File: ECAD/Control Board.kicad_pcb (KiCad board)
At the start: 2 copper layers, 184.2 x 57.8 mm, 60 parts, among them J3 Thermocouple, J4 SD_Card, J5 PWR/Heat, J7 UPDI, Q1 IPD50N06S4L08, SW1 Reflow, SW2 Stop, SW3 Set temp mode, U1 ATtiny1614-SS, U2 TPS7B8833QKVURQ1, U3 AD8497, U4 HT16K33

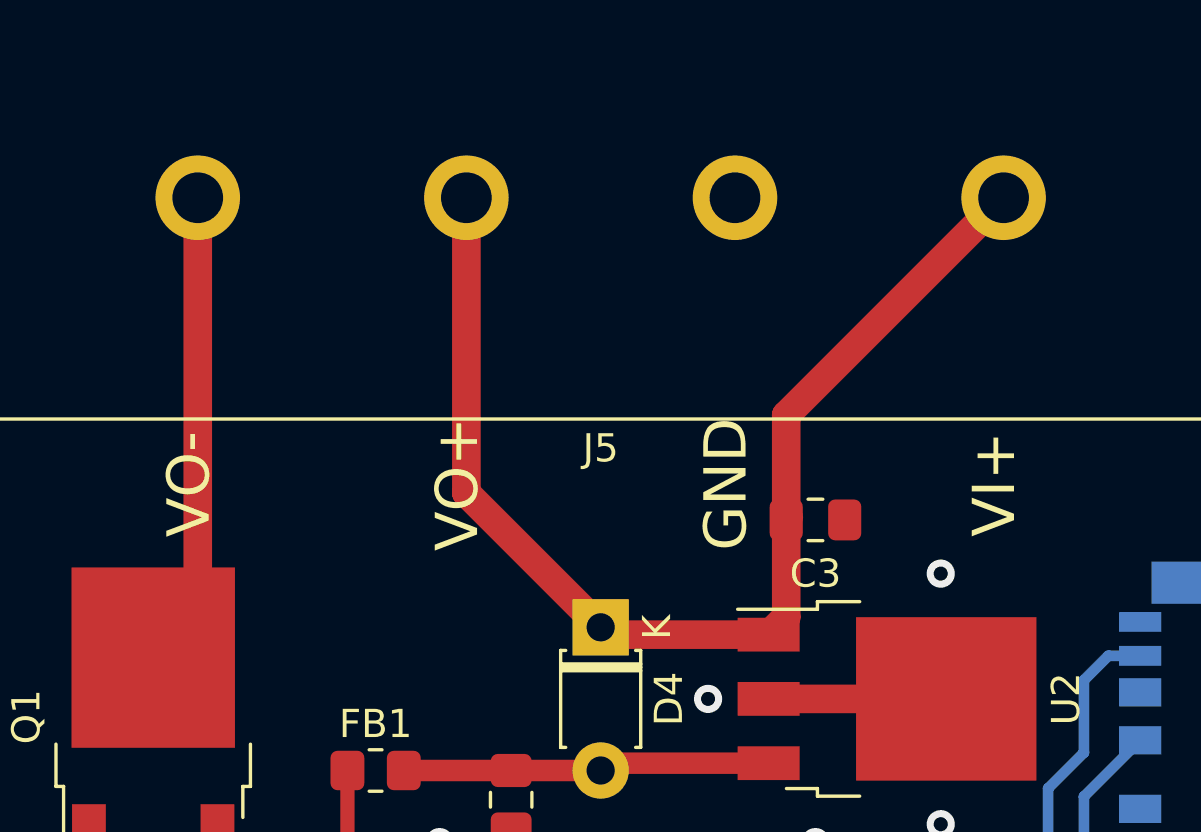
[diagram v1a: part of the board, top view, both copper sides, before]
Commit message: High voltage modifications
Widened high voltage tracks and replaced schottky diode with higher back voltage diode.
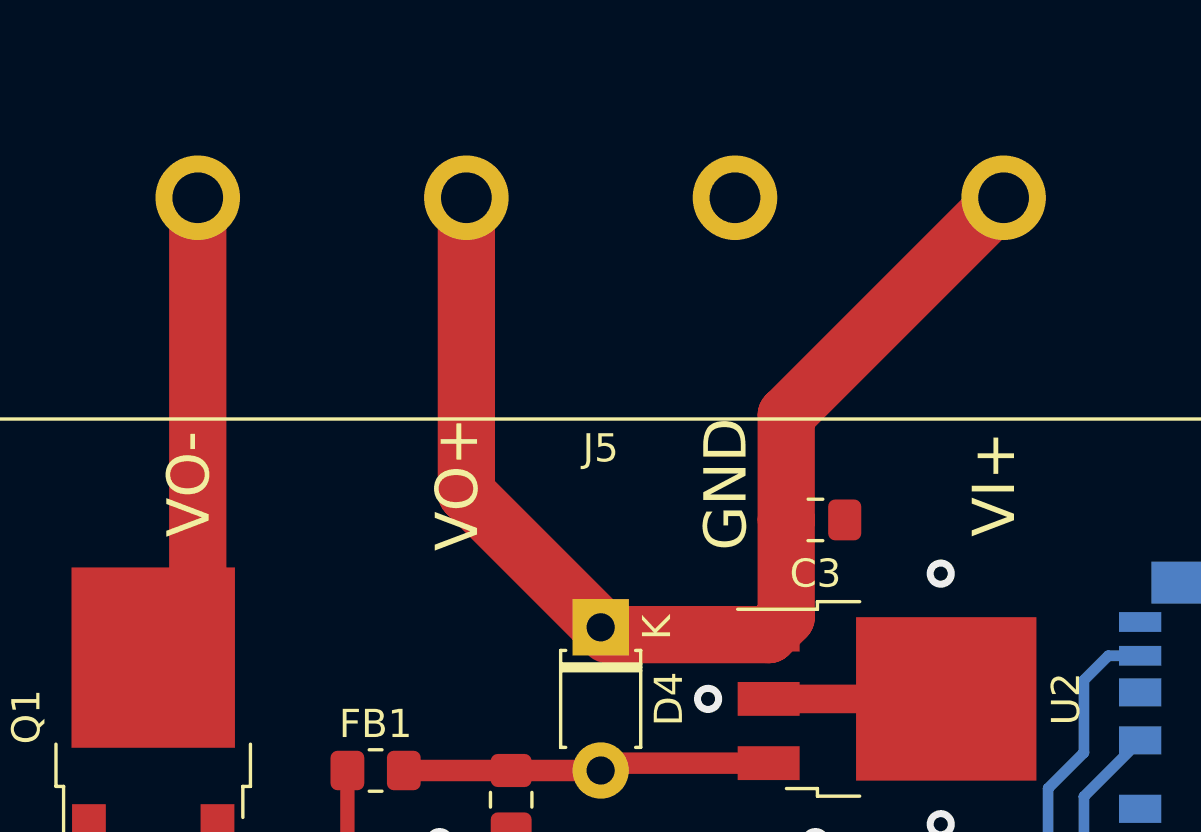
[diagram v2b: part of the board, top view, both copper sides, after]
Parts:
- D4: value 1N5818 -> 1N5711
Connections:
- DS1 pad 3: (no net) -> Net-(DS1-Pad3)
- DS2 pad 3: (no net) -> Net-(DS2-Pad3)
- DS3 pad 3: (no net) -> Net-(DS3-Pad3)
- J4 pad 11: (no net) -> /WRPrt
- J4 pad 8: (no net) -> Net-(J4-Pad8)
- J4 pad 9: (no net) -> Net-(J4-Pad9)
- U1 pad 6: (no net) -> Net-(U1-Pad6)
- U3 pad 4: (no net) -> Net-(U3-Pad4)
- U4 pad 10: (no net) -> Net-(U4-Pad10)
- U4 pad 11: (no net) -> Net-(U4-Pad11)
- U4 pad 8: (no net) -> Net-(U4-Pad8)
- U4 pad 9: (no net) -> Net-(U4-Pad9)

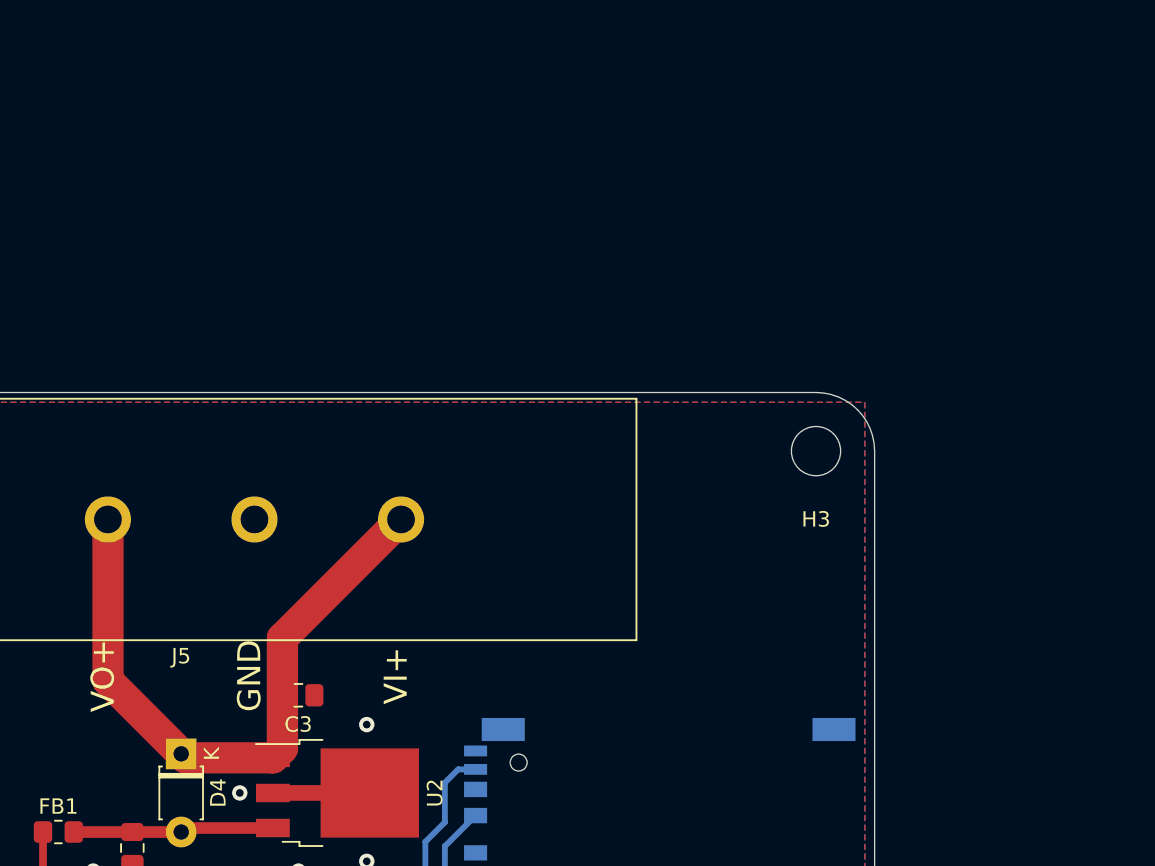
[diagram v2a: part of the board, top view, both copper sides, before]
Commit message: Added footprints to board
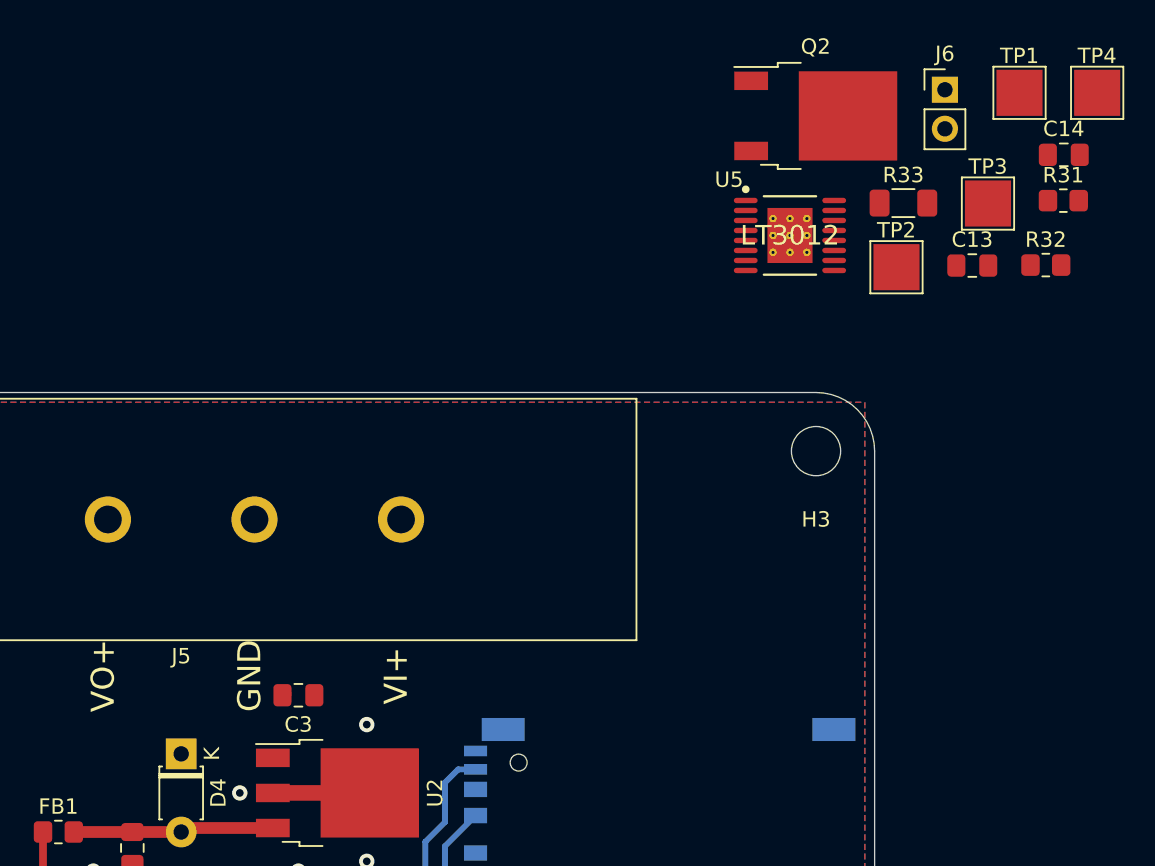
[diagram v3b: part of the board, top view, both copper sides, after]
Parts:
- added C13: 1uF, Capacitor_SMD:C_0805_2012Metric_Pad1.18x1.45mm_HandSolder, F.Cu at (240.0, 37.5)
- added C14: 4.7uF, Capacitor_SMD:C_0805_2012Metric_Pad1.18x1.45mm_HandSolder, F.Cu at (246.0, 30.3)
- added J6: FAN, Connector_PinHeader_2.54mm:PinHeader_1x02_P2.54mm_Vertical, F.Cu at (238.2, 26.0)
- added Q2: IPD50N06S4L08, Package_TO_SOT_SMD:TO-252-2, F.Cu at (229.8, 27.7)
- added R31: 1.74M, Resistor_SMD:R_0805_2012Metric_Pad1.20x1.40mm_HandSolder, F.Cu at (245.9, 33.2)
- added R32: 200K, Resistor_SMD:R_0805_2012Metric_Pad1.20x1.40mm_HandSolder, F.Cu at (244.8, 37.4)
- added R33: 100R, Resistor_SMD:R_1206_3216Metric_Pad1.30x1.75mm_HandSolder, F.Cu at (235.6, 33.4)
- added TP1: VIN, TestPoint:TestPoint_Pad_3.0x3.0mm, F.Cu at (243.1, 26.2)
- added TP2: 12V, TestPoint:TestPoint_Pad_3.0x3.0mm, F.Cu at (235.1, 37.6)
- added TP3: 3.3V, TestPoint:TestPoint_Pad_3.0x3.0mm, F.Cu at (241.1, 33.4)
- added TP4: GND, TestPoint:TestPoint_Pad_3.0x3.0mm, F.Cu at (248.2, 26.2)
- added U5: LT3012, PCB Heater:Linear_Technology-LT3012EFETRPBF-Level_B, F.Cu at (228.2, 35.5)
- C3: value 1uF -> 10uF
- U2: value TPS7B8833QKVURQ1 -> LD1086DT33
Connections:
- C3 pad 1: VCC -> +12V
- D4 pad 1: VCC -> +12V
- U1 pad 6: Net-(U1-Pad6) -> /FanPWM
- U2 pad 1: VCC -> +12V
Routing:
- net VCC: track 42.4 -> 0.00 mm

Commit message: Re-arrange components
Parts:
- TP1, TP2, TP3, TP4: footprint TestPoint:TestPoint_Pad_3.0x3.0mm -> TestPoint:TestPoint_Pad_2.0x2.0mm
- moved J6 196.1 mm to (52.1, 87.6)
- moved R33 185.5 mm to (54.4, 73.2)
- moved Q2 179.6 mm to (57.8, 79.4)
- moved TP2 33.5 mm to (258.6, 13.7)
- moved TP3 23.2 mm to (258.6, 18.3)
- moved TP1 23.1 mm to (258.6, 9.14)
- moved C13 20.1 mm to (220.0, 38.1), turned to 270 degrees
- moved R31 12.5 mm to (234.7, 38.6), turned to 270 degrees
- moved R32 12.2 mm to (234.7, 44.2), turned to 270 degrees
- moved TP4 11.0 mm to (258.6, 22.9)
- moved C14 8.89 mm to (245.4, 39.1), turned to 270 degrees
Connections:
- DS1 pad 3: Net-(DS1-Pad3) -> (no net)
- DS2 pad 3: Net-(DS2-Pad3) -> (no net)
- DS3 pad 3: Net-(DS3-Pad3) -> (no net)
- J4 pad 11: /WRPrt -> (no net)
- J4 pad 8: Net-(J4-Pad8) -> (no net)
- J4 pad 9: Net-(J4-Pad9) -> (no net)
- J5 pad 1: /H- -> GND
- J5 pad 2: VCC -> /H-
- J5 pad 3: GND -> VCC
- U3 pad 4: Net-(U3-Pad4) -> (no net)
- U4 pad 10: Net-(U4-Pad10) -> (no net)
- U4 pad 11: Net-(U4-Pad11) -> (no net)
- U4 pad 8: Net-(U4-Pad8) -> (no net)
- U4 pad 9: Net-(U4-Pad9) -> (no net)
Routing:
- net /H-: track 17.0 -> 0.00 mm
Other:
- board text added: "PCB Heater Control Board Rev 0.3"
- board text removed: "PCB Heater Control Board Rev 0.2"

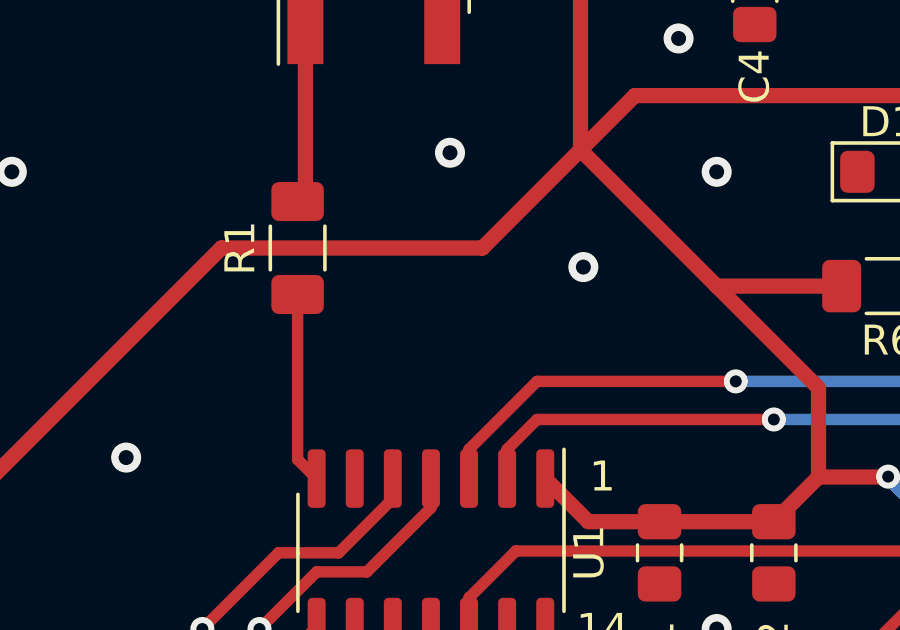
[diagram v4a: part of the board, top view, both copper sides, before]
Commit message: Added pulldown to mosfet gate
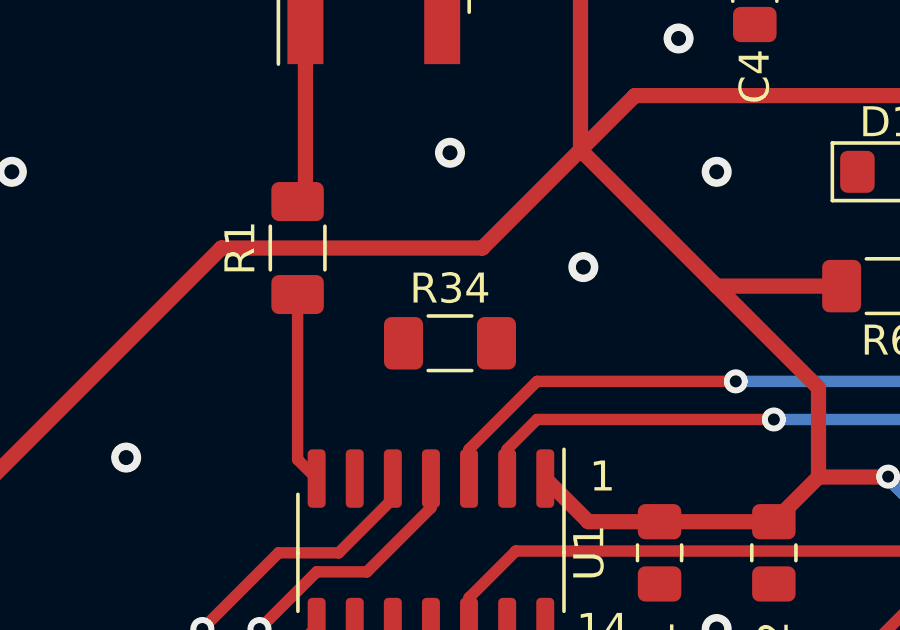
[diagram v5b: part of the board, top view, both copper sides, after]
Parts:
- added R34: 10K, Resistor_SMD:R_1206_3216Metric_Pad1.30x1.75mm_HandSolder, F.Cu at (175.3, 87.0)

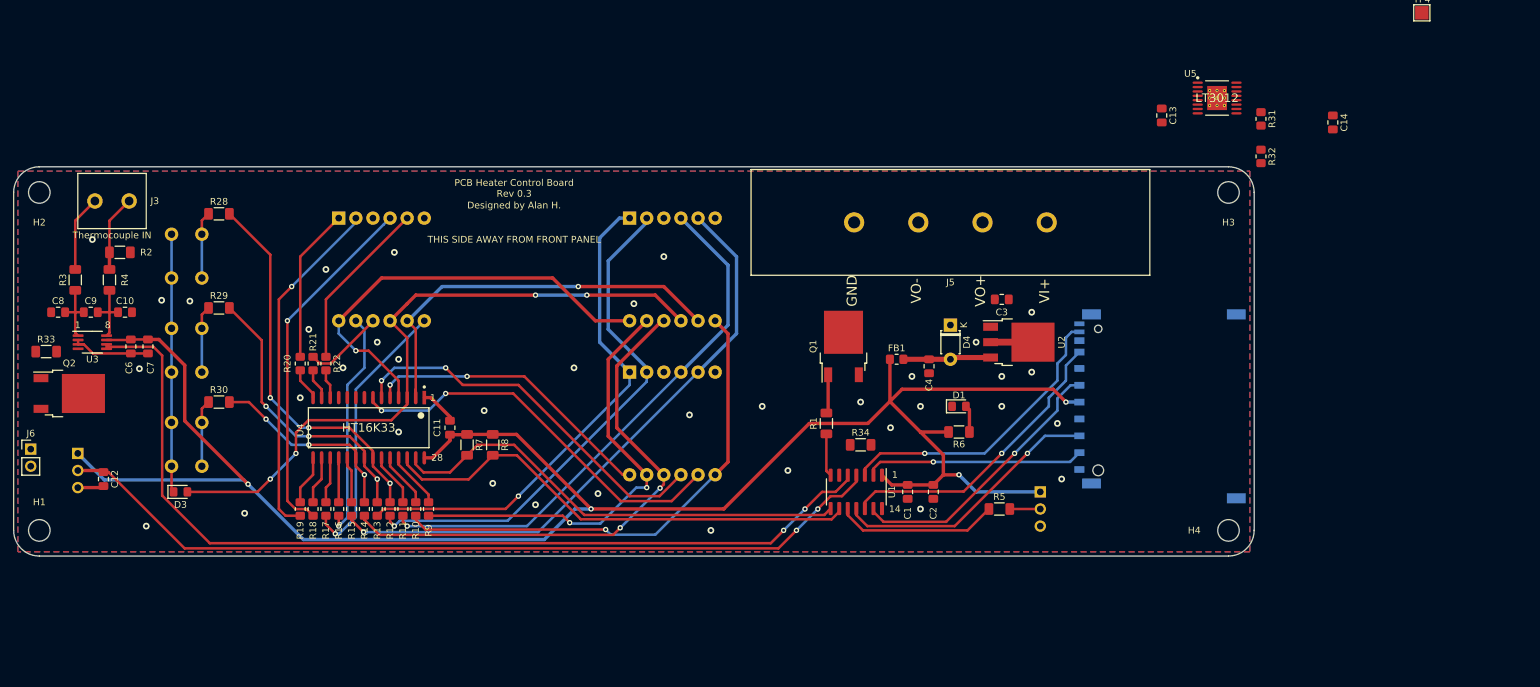
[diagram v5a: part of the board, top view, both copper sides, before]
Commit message: Replaced primary LDO with LM317
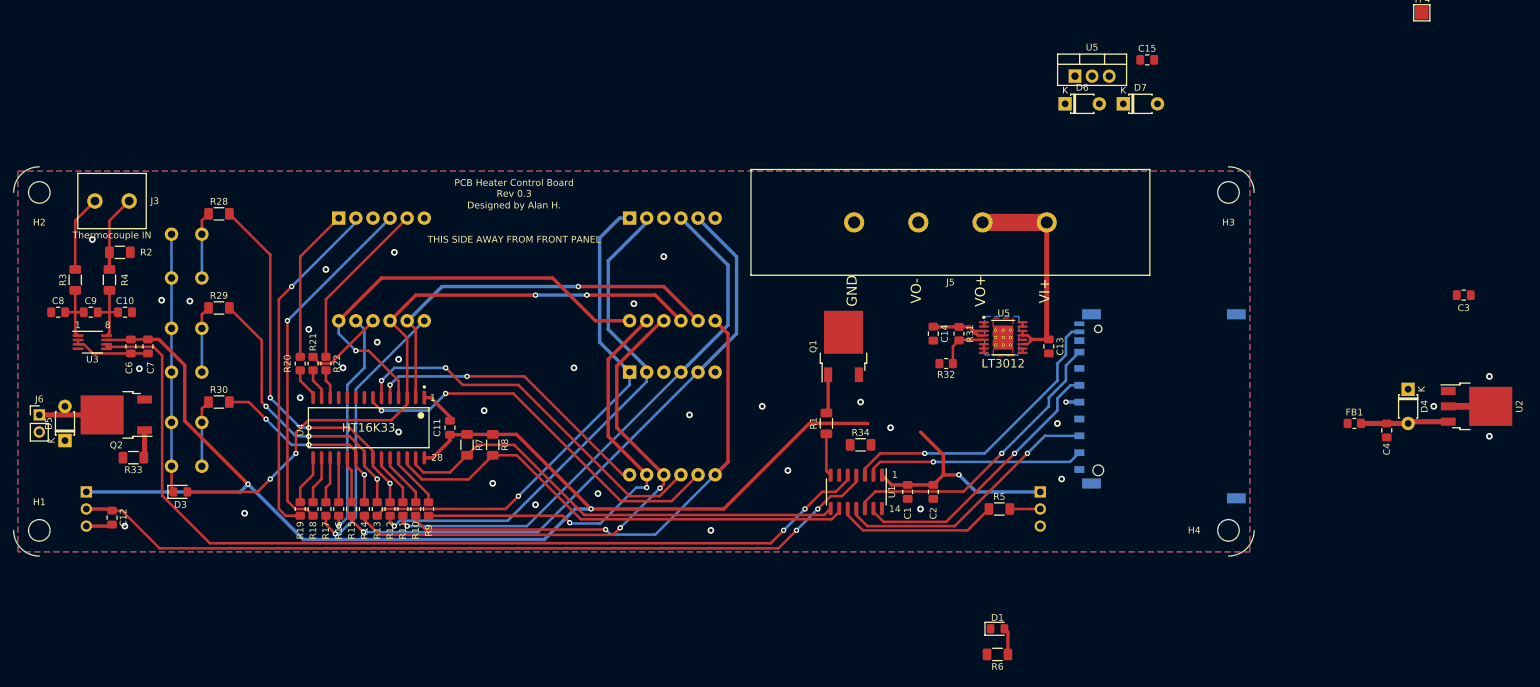
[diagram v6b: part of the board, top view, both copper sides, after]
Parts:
- removed the U5 at (228.2, 35.5)
- added C15: 10uF, Capacitor_SMD:C_0805_2012Metric_Pad1.18x1.45mm_HandSolder, F.Cu at (217.8, 29.8)
- added D5: 1N4001, Diode_THT:D_T-1_P5.08mm_Horizontal, F.Cu at (57.1, 86.4)
- added D6: 1N4002, Diode_THT:D_T-1_P5.08mm_Horizontal, F.Cu at (205.6, 36.4)
- added D7: 1N4001, Diode_THT:D_T-1_P5.08mm_Horizontal, F.Cu at (214.3, 36.4)
- added U5: LM317, Package_TO_SOT_THT:TO-220-3_Vertical, F.Cu at (207.1, 32.3)
- added U5: LT3012, PCB Heater:Linear_Technology-LT3012EFETRPBF-Level_B, F.Cu at (196.4, 71.1)
- C13: value 1uF -> 0.1uF
- R31: value 1.74M -> 240R
- R32: value 200K -> 2.1K
- moved C4 68.6 mm to (253.4, 84.9)
- moved D4 68.6 mm to (256.5, 78.7)
- moved U2 68.6 mm to (266.7, 81.3)
- moved FB1 68.6 mm to (248.6, 83.8)
- moved C3 68.6 mm to (264.8, 64.8)
- moved C14 67.1 mm to (186.1, 70.5)
- moved R32 55.9 mm to (188.0, 74.9), turned to 180 degrees
- moved R31 55.0 mm to (189.9, 70.5)
- moved C13 38.2 mm to (203.2, 72.4)
- moved D1 33.5 mm to (195.6, 114.3)
- moved R6 33.5 mm to (195.6, 118.1)
- moved R33 20.4 mm to (67.3, 88.9), turned to 180 degrees
- moved Q2 7.67 mm to (64.8, 82.5), turned to 180 degrees
- moved C12 5.85 mm to (64.1, 97.8)
- moved RV1 5.85 mm to (60.3, 94.0)
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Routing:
- net +3V3: track 280.4 -> 228.5 mm
- net VCC: track 0.00 -> 33.5 mm
- net +12V: track 0.50 -> 10.9 mm
- net Net-(D5-Pad2): track 0.00 -> 9.33 mm
- net Net-(R31-Pad2): track 0.00 -> 7.54 mm
- net Net-(Q2-Pad1): track 0.00 -> 4.12 mm
- net /TempCtrl: track 125.4 -> 121.8 mm
- net GND: track 27.4 -> 30.6 mm, vias 35 -> 31

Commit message: Associate footprints and update board
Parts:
- removed D7: 1N4001, Diode_THT:D_T-1_P5.08mm_Horizontal
- removed the U5 at (207.1, 32.3)
- removed the U5 at (196.4, 71.1)
- added L1: 470uH, Inductor_SMD:L_12x12mm_H8mm, F.Cu at (293.3, 39.5)
- added U5: LM2575HVS-ADJ, Package_TO_SOT_SMD:TO-263-5_TabPin3, F.Cu at (277.0, 38.6)
- C13: value 0.1uF -> 100uF; footprint Capacitor_SMD:C_0805_2012Metric_Pad1.18x1.45mm_HandSolder -> Capacitor_SMD:CP_Elec_10x10.5
- C14: value 4.7uF -> 470uF; footprint Capacitor_SMD:C_0805_2012Metric_Pad1.18x1.45mm_HandSolder -> Capacitor_SMD:CP_Elec_8x10.5
- C15: value 10uF -> 22uF
- D4: value 1N5711 -> 1N5818
- D6: value 1N4002 -> 1N5818
- R31: value 240R -> 1K
- R32: value 2.1K -> 3.1K
- TP2: value 12V -> 5V
- moved R32 125.4 mm to (307.8, 38.0), turned to 0 degrees
- moved R31 110.9 mm to (298.5, 48.1), turned to 0 degrees
- moved C14 105.1 mm to (289.4, 51.7), turned to 0 degrees
- moved D6 96.8 mm to (302.4, 34.5)
- moved C15 85.6 mm to (303.0, 38.1)
- moved C13 75.5 mm to (275.6, 50.8), turned to 0 degrees
- moved H1 50.2 mm to (53.3, 49.5)
- moved H2 50.2 mm to (53.3, 99.7)
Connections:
- C14 pad 1: +12V -> +5V
- C15 pad 1: Net-(C15-Pad1) -> +5V
- C3 pad 1: +12V -> +5V
- D4 pad 1: +12V -> +5V
- D5 pad 1: +12V -> +5V
- D6 pad 1: VCC -> Net-(D6-Pad1)
- D6 pad 2: +12V -> GND
- J6 pad 2: +12V -> +5V
- R31 pad 1: +12V -> Net-(R31-Pad1)
- R31 pad 2: Net-(C15-Pad1) -> GND
- R32 pad 1: Net-(C15-Pad1) -> +5V
- R32 pad 2: GND -> Net-(R31-Pad1)
- TP2 pad 1: +12V -> +5V
- U2 pad 1: +12V -> +5V
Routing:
- net VCC: track 33.5 -> 9.53 mm
- net +12V: track 10.9 -> 0.00 mm
- net Net-(R31-Pad2): track 7.54 -> 0.00 mm
- net GND: track 30.6 -> 27.4 mm
